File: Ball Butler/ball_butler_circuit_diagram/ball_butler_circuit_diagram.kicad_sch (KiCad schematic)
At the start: 13 parts

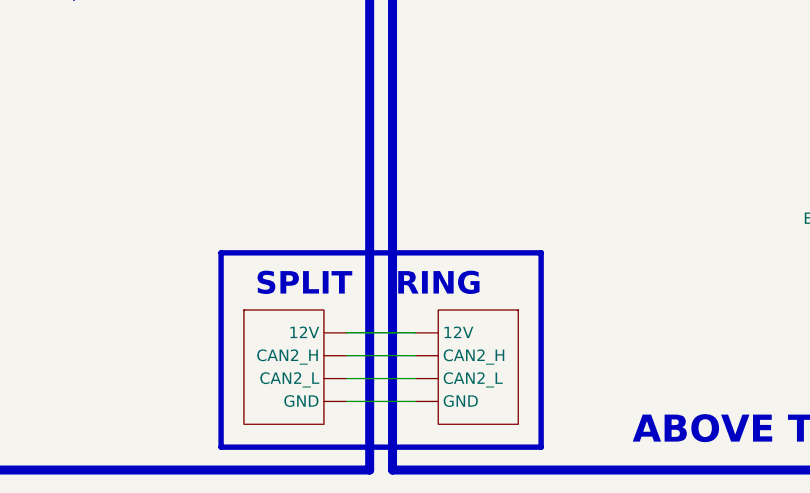
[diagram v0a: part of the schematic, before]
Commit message: Correct "Slip Ring" Typo
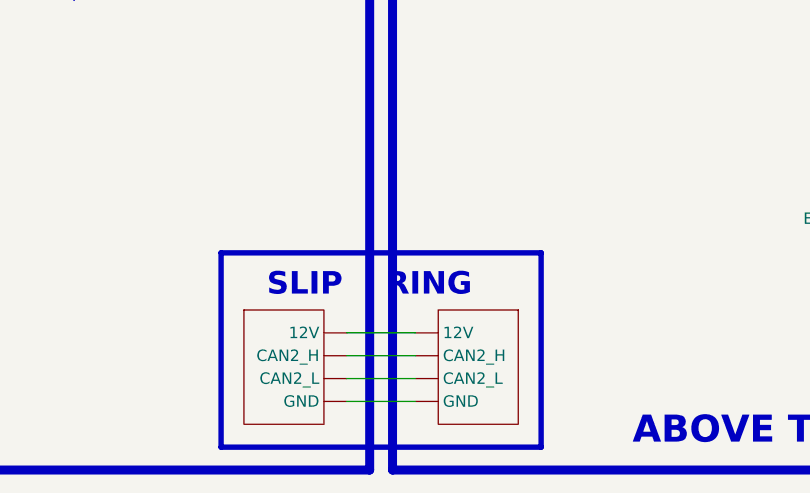
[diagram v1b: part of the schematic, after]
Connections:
- net at U?. (NC): now also U?. (VIN)
- new net: U?. (GND), U?. (GND) (x3)
- new net: M?. (C), U?. (VIN) (x2)
- new net: M?. (PWR2), U?. (VIN)
- new net: U?. (NC), U?. (VIN) (x4)
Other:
- note added: "SLIP RING"
- note removed: "SPLIT RING"
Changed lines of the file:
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@@
     (effects (font (size 1.5 1.5)) (justify left bottom))
   )
-  (text "SPLIT    RING" (at 175.26 144.78 0)
+  (text "SLIP    RING" (at 176.53 144.78 0)
     (effects (font (size 2.5 2.5) bold) (justify left bottom))
   )

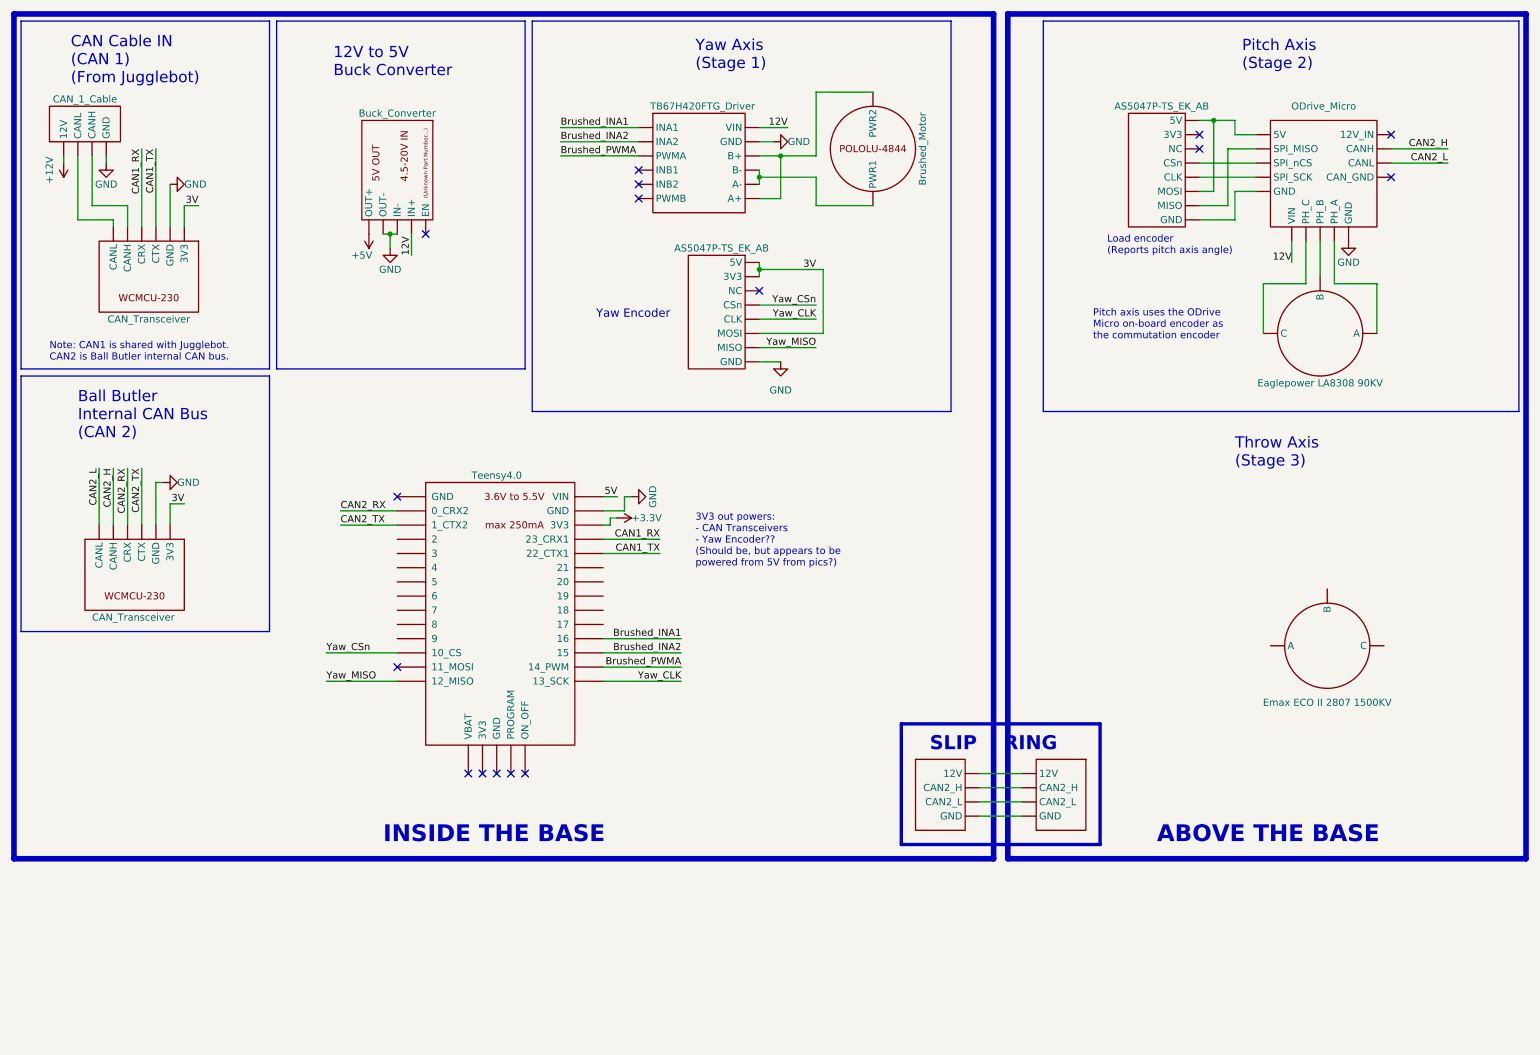
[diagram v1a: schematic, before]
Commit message: Update circuit diagram to include programming logic and PWR/CAN
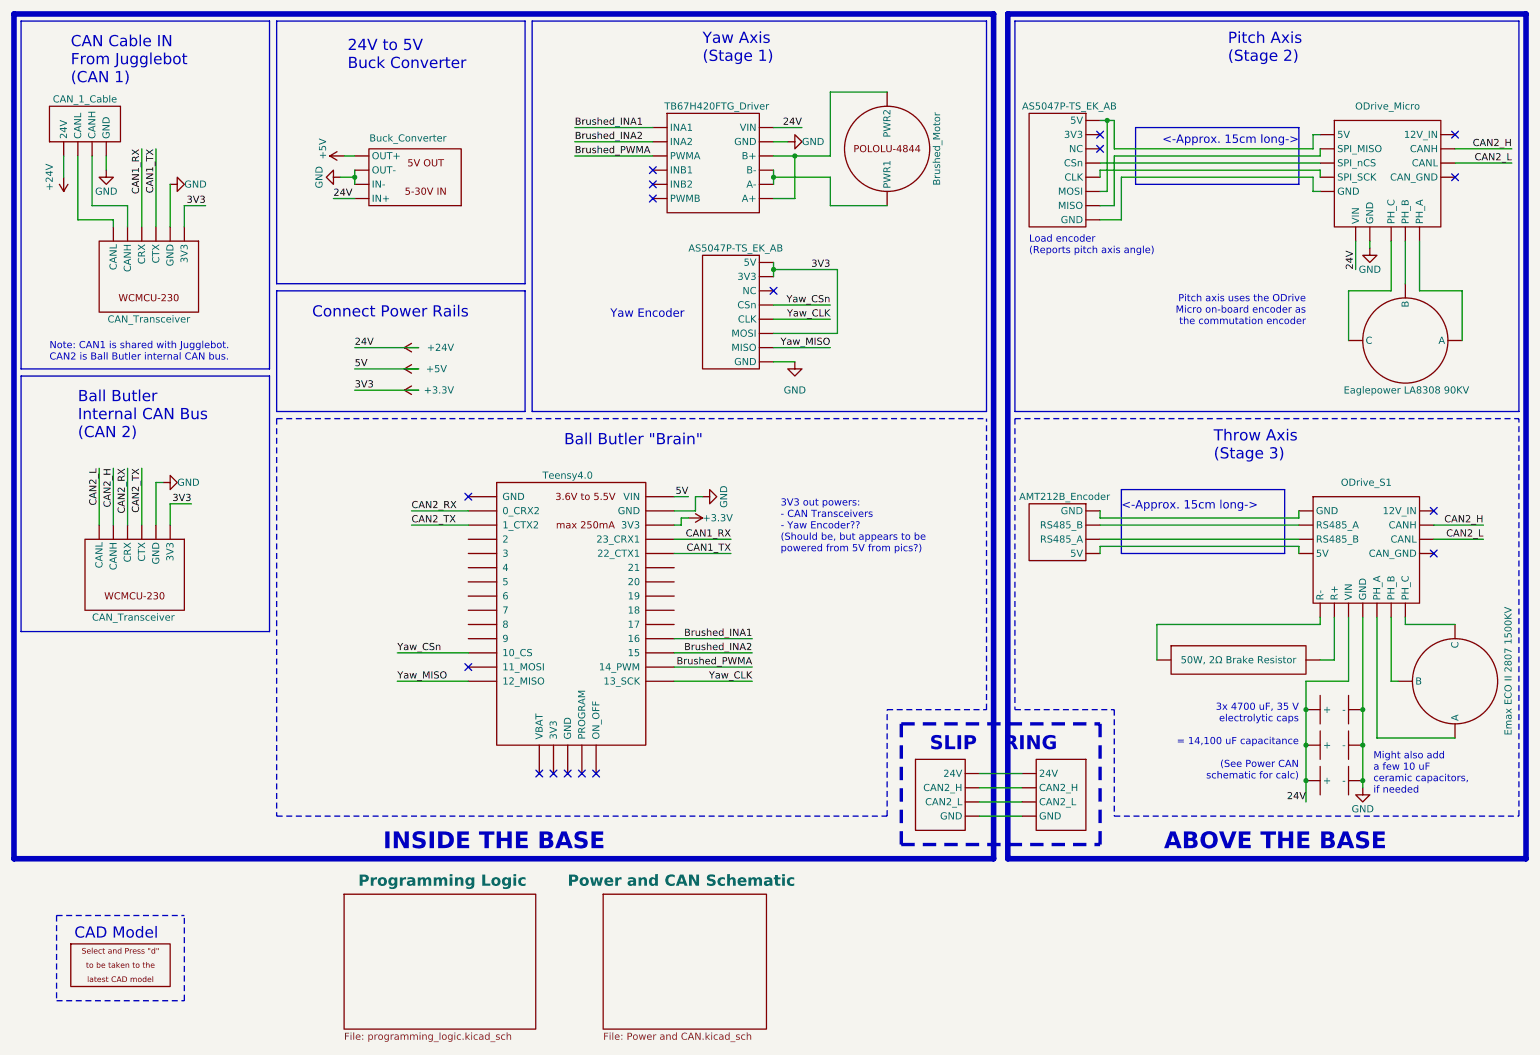
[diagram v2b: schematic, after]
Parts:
- added U?: ODrive_S1, symbol Ball_Butler_Symbol_Library:ODrive_S1
- added U? (x3): 4700 uF, 35V Capacitor, symbol Ball_Butler_Symbol_Library:4700 uF, 35V Capacitor
- added U?: AMT212B_Encoder, symbol Ball_Butler_Symbol_Library:AMT212B_Encoder
- added U?: zCAD_Model, symbol Ball_Butler_Symbol_Library:zCAD_Model
- added U?: 50W, 2Ω Brake Resistor, symbol Ball_Butler_Symbol_Library:50W, 2Ω Brake Resistor
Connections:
- net 12V is gone; now on net GND: U?. (OUT-), U?. (VIN), U?. (VIN)
- net 5V is gone; now on net +5V: U?.33 (VIN)
- net +3.3V: now also U?. (GND), U?. (GND), U?. (NC)
- net CAN2_H: now also U?. (VIN)
- net CAN2_L: now also U?. (VIN)
- net GND: now also U?. (-), U?. (-), U?. (-), U?. (VIN)
- net at M?. (C): now also U?. (VIN)
- net at U?. (NC): now also U?. (VIN)
- removed net 3V: U?. (GND), U?. (GND), U?. (NC)
- new net: U?. (GND), U?. (GND) (x3)
- new net: M?. (C), U?. (VIN) (x4)
- new net: U?. (RS485_B), U?. (VIN) (x4)
- new net: U?. (PIN), U?. (VIN) (x2)
- new net: M?. (PWR2), U?. (VIN)
- new net: U?. (NC), U?. (VIN) (x4)
- new net +24V: U?. (-), U?. (-), U?. (-), U?. (OUT-), U?. (VIN), U?. (VIN), U?. (VIN)
- no-connect marks 16 -> 17
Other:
- added sheet Power and CAN Schematic (Power and CAN.kicad_sch)
- added sheet Programming Logic (programming_logic.kicad_sch)
- note added: "24V to 5V Buck Converter"
- note added: "3x 4700 uF, 35 V electrolytic caps = 14,100 uF capacitance (See Power CAN schematic for calc)"
- note added: "<-Approx. 15cm long->"
- note added: "Ball Butler "Brain""
- note added: "CAD Model"
- note added: "CAN Cable IN From Jugglebot (CAN 1)"
- note added: "Connect Power Rails"
- note added: "Might also add a few 10 uF ceramic capacitors, if needed"
- note removed: "12V to 5V Buck Converter"
- note removed: "CAN Cable IN (CAN 1) (From Jugglebot)"

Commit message: Minor update to schematic
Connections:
- net at U?. (NC): now also U?. (VIN)
- new net: U?. (GND), U?. (GND) (x3)
- new net: M?. (C), U?. (VIN) (x4)
- new net: U?. (RS485_B), U?. (VIN) (x3)
- new net: U?. (PIN), U?. (VIN)
- new net: M?. (PWR2), U?. (VIN)
- new net: U?. (NC), U?. (VIN) (x4)
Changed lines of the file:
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@@
       (reference "U?") (unit 1) (value "50W, 2Ω Brake Resistor") (footprint "")
+    )
+    (path "/f47f7cdf-3580-439c-86a6-80f9e434af39/f2ca9f06-88e8-42cc-a39c-22b7c0813816"
+      (reference "U?") (unit 1) (value "throw_scheduler") (footprint "")
     )
     (path "/8ed858a8-e638-495c-b31c-77c4342d4bce/f2eeebc6-0e67-44f9-963a-7f2e6a51294e"

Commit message: Update circuit diagram
Add ROS -> CAN1 = CAN2
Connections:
- net CAN2_H is gone; now on net GND: U?. (GND), U?. (VIN), U?. (VIN)
- net CAN2_L is gone; now on net GND: U?. (GND), U?. (VIN), U?. (VIN)
- net at U?. (NC): now also U?. (VIN)
- new net: U?. (GND), U?. (GND) (x3)
- new net: M?. (C), U?. (VIN) (x4)
- new net: U?. (RS485_B), U?. (VIN) (x3)
- new net: U?. (PIN), U?. (VIN)
- new net: M?. (PWR2), U?. (VIN)
- new net: U?. (NC), U?. (VIN) (x4)
- new net CAN1_H: U?. (GND), U?. (VIN), U?. (VIN)
- new net CAN1_L: U?. (GND), U?. (VIN), U?. (VIN)
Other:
- note added: "Not In Use (CAN1 = CAN2)"
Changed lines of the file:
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@@
     (stroke (width 0) (type default) (color 0 0 0 0))
+  )
+  (polyline (pts (xy 19.05 92.71) (xy 53.34 118.11))
+    (stroke (width 2) (type solid) (color 255 0 0 1))
   )
   (polyline (pts (xy 59.69 62.23) (xy 59.69 83.82))
@@
     (stroke (width 0) (type default) (color 0 0 0 0))
   )
+  (polyline (pts (xy 82.55 105.41) (xy 92.71 97.79))
+    (stroke (width 1) (type solid) (color 255 0 0 1))
+  )
   (wire (pts (xy 207.01 107.95) (xy 207.01 109.22))
     (stroke (width 0) (type default) (color 255 0 0 1))
@@
     (stroke (width 0.2) (type dash) (color 255 0 0 1))
   )
+  (polyline (pts (xy 82.55 97.79) (xy 92.71 105.41))
+    (stroke (width 1) (type solid) (color 255 0 0 1))
+  )
   (wire (pts (xy 38.1 96.52) (xy 38.1 104.14))
     (stroke (width 0) (type default) (color 0 0 0 1))
@@
     (stroke (width 0) (type default) (color 0 0 0 0))
   )
+  (polyline (pts (xy 19.05 118.11) (xy 53.34 92.71))
+    (stroke (width 2) (type solid) (color 255 0 0 1))
+  )
   (wire (pts (xy 73.66 45.72) (xy 69.85 45.72))
     (stroke (width 0.3) (type default) (color 255 0 0 1))
@@
     (stroke (width 0) (type default) (color 0 255 0 1))
   )
-  (polyline (pts (xy 13.97 123.19) (xy 58.42 123.19))
+  (polyline (pts (xy 13.97 144.78) (xy 58.42 144.78))
     (stroke (width 0.2) (type default) (color 255 0 0 1))
   )
@@
     (stroke (width 0.3) (type default) (color 0 0 0 1))
   )
-  (polyline (pts (xy 58.42 123.19) (xy 58.42 77.47))
+  (polyline (pts (xy 58.42 144.78) (xy 58.42 77.47))
     (stroke (width 0.2) (type default) (color 255 0 0 1))
   )
@@
     (stroke (width 0) (type default) (color 0 0 0 0))
   )
+  (wire (pts (xy 26.67 138.43) (xy 43.18 138.43))
+    (stroke (width 0) (type default) (color 0 255 0 1))
+  )
   (polyline (pts (xy 240.03 109.22) (xy 240.03 97.79))
     (stroke (width 0) (type default) (color 0 0 0 0))
@@
     (stroke (width 0) (type default) (color 0 0 0 0))
   )
+  (wire (pts (xy 26.67 134.62) (xy 43.18 134.62))
+    (stroke (width 0) (type default) (color 255 255 0 1))
+  )
   (wire (pts (xy 251.46 62.23) (xy 251.46 71.12))
     (stroke (width 0) (type default) (color 0 0 0 0))
@@
     (stroke (width 0) (type default) (color 0 0 0 1))
   )
-  (polyline (pts (xy 13.97 77.47) (xy 13.97 123.19))
+  (polyline (pts (xy 13.97 77.47) (xy 13.97 144.78))
     (stroke (width 0.2) (type default) (color 255 0 0 1))
   )
@@
     (effects (font (size 1.27 1.27)) (justify left bottom))
   )
+  (text "Not In Use\n(CAN1 = CAN2)" (at 24.13 129.54 0)
+    (effects (font (size 2 2) (thickness 0.4) bold) (justify left bottom))
+  )
   (text "INSIDE THE BASE" (at 78.74 162.56 0)
     (effects (font (size 3 3) (thickness 0.6) bold) (justify left bottom))
@@
     (effects (font (size 1.27 1.27)) (justify right bottom))
   )
+  (label "CAN2_H" (at 43.18 134.62 180)
+    (effects (font (size 1.27 1.27)) (justify right bottom))
+  )
   (label "3V3" (at 44.45 100.33 180)
     (effects (font (size 1.27 1.27)) (justify right bottom))
@@
     (effects (font (size 1.27 1.27)) (justify right bottom))
   )
+  (label "CAN2_L" (at 43.18 138.43 180)
+    (effects (font (size 1.27 1.27)) (justify right bottom))
+  )
   (label "CAN2_H" (at 275.59 104.14 180)
     (effects (font (size 1.27 1.27)) (justify right bottom))
@@
     (effects (font (size 1.27 1.27)) (justify right bottom))
   )
+  (label "CAN1_L" (at 26.67 138.43 0)
+    (effects (font (size 1.27 1.27)) (justify left bottom))
+  )
   (label "Yaw_CSn" (at 81.28 127 0)
     (effects (font (size 1.27 1.27)) (justify left bottom))
@@
   (label "CAN1_RX" (at 35.56 36.83 270)
     (effects (font (size 1.27 1.27)) (justify right bottom))
+  )
+  (label "CAN1_H" (at 26.67 134.62 0)
+    (effects (font (size 1.27 1.27)) (justify left bottom))
   )
   (label "3V3" (at 73.66 80.01 0)
@@
       (reference "#PWR?") (unit 1) (value "GND") (footprint "")
     )
+    (path "/8ed858a8-e638-495c-b31c-77c4342d4bce/2c6a38d8-8a23-44c0-86e8-b45d80dce059"
+      (reference "#PWR?") (unit 1) (value "Earth") (footprint "")
+    )
     (path "/51cf1321-827b-4c6e-8b53-4afb19388a7d"
       (reference "#PWR?") (unit 1) (value "GND") (footprint "")
@@
       (reference "#PWR?") (unit 1) (value "+24V") (footprint "")
     )
+    (path "/8ed858a8-e638-495c-b31c-77c4342d4bce/b2c9f62c-f2c7-4ade-965a-e0130848f3dd"
+      (reference "#PWR?") (unit 1) (value "Earth") (footprint "")
+    )
     (path "/d40f7c7c-70a2-4c3c-b688-4ca22d2c113c"
       (reference "#PWR?") (unit 1) (value "GND") (footprint "")
@@
       (reference "U?") (unit 1) (value "45V 12.5A PSU") (footprint "")
     )
+    (path "/f47f7cdf-3580-439c-86a6-80f9e434af39/20395ea7-59ae-452e-9250-0e0b18719f6f"
+      (reference "U?") (unit 1) (value "can1_receiver") (footprint "")
+    )
     (path "/f47f7cdf-3580-439c-86a6-80f9e434af39/24b6e83c-fa1f-4658-a814-2d4625a7322c"
       (reference "U?") (unit 1) (value "store_throw_num") (footprint "")
     )
-    (path "/f47f7cdf-3580-439c-86a6-80f9e434af39/27c75258-0d14-4597-8384-4b35e41081d2"
-      (reference "U?") (unit 1) (value "CAN_Frame") (footprint "")
-    )
     (path "/3005be57-9842-4134-96d2-a3e5d7976d31"
       (reference "U?") (unit 1) (value "TB67H420FTG_Driver") (footprint "")
@@
       (reference "U?") (unit 1) (value "4700 uF, 35V Capacitor") (footprint "")
     )
-    (path "/f47f7cdf-3580-439c-86a6-80f9e434af39/345bfd28-4c52-42b1-9a28-939e7a993398"
-      (reference "U?") (unit 1) (value "CRC_calculator") (footprint "")
-    )
     (path "/8ed858a8-e638-495c-b31c-77c4342d4bce/37372327-c8a2-48cc-8bca-bfbada9e2ff8"
       (reference "U?") (unit 1) (value "ODrive Pro 1") (footprint "")
@@
       (reference "U?") (unit 1) (value "can1_transmitter") (footprint "")
     )
-    (path "/f47f7cdf-3580-439c-86a6-80f9e434af39/8382bef6-c5f8-4ca6-86d3-ceb28bfae123"
-      (reference "U?") (unit 1) (value "proprioception_handler") (footprint "")
-    )
     (path "/f47f7cdf-3580-439c-86a6-80f9e434af39/976d4190-3ffb-4a7d-9f5d-de19a9216559"
       (reference "U?") (unit 1) (value "IK_solver") (footprint "")
@@
       (reference "U?") (unit 1) (value "ODrive Pro 0") (footprint "")
     )
+    (path "/f47f7cdf-3580-439c-86a6-80f9e434af39/bc713a15-7589-4b7e-9856-ab74036af036"
+      (reference "U?") (unit 1) (value "CAN_Frame") (footprint "")
+    )
     (path "/f47f7cdf-3580-439c-86a6-80f9e434af39/bd272f74-5169-48aa-b1af-95e0b50f6ffa"
       (reference "U?") (unit 1) (value "hand_trajectory_planner") (footprint "")
@@
       (reference "U?") (unit 1) (value "12V 5A PSU") (footprint "")
     )
-    (path "/f47f7cdf-3580-439c-86a6-80f9e434af39/fc94f80f-83a2-4306-af16-a108a97dcb30"
-      (reference "U?") (unit 1) (value "CAN_Frame") (footprint "")
-    )
-    (path "/f47f7cdf-3580-439c-86a6-80f9e434af39/fcee52d0-b1c3-42c9-960d-bc532ebf1202"
-      (reference "U?") (unit 1) (value "CAN_Frame") (footprint "")
-    )
     (path "/fe4deba2-ab05-4123-abe4-c1d51bba2b57"

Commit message: Update circuit diagram
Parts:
- removed U? (x3): 4700 uF, 35V Capacitor, symbol Ball_Butler_Symbol_Library:4700 uF, 35V Capacitor
- removed U?: AMT212B_Encoder, symbol Ball_Butler_Symbol_Library:AMT212B_Encoder
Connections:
- net at U?. (NC): now also U?. (VIN)
- new net: U?. (GND), U?. (GND) (x3)
- new net: M?. (C), U?. (VIN) (x4)
- new net: U?. (PIN), U?. (VIN)
- new net: M?. (PWR2), U?. (VIN)
- new net: U?. (NC), U?. (VIN) (x4)
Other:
- note added: "3V3 out powers: - CAN Transceiver - Yaw Encoder"
- note added: "CAN Node 7"
- note added: "CAN Node 8"
- note added: "Throw axis uses the ODrive S1 on-board encoder as the commutation encoder"
- note removed: "3V3 out powers: - CAN Transceivers - Yaw Encoder?? (Should be, but appears to be powered from 5V from pics?)"
- note removed: "3x 4700 uF, 35 V electrolytic caps = 14,100 uF capacitance (See Power CAN schematic for calc)"
- note removed: "Might also add a few 10 uF ceramic capacitors, if needed"
